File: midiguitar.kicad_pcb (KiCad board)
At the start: 2 copper layers, 64.9 x 24.8 mm, 12 parts, among them M1 ESP32S3, P1 Conn_USB_A_Plug, SW1 Switch_Slide_1, SW2 Switch_Slide_1, U1 Regulator_Linear_3.3V_1A_Diod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, U2 LevelShifter_Texas_TXB0104DR_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

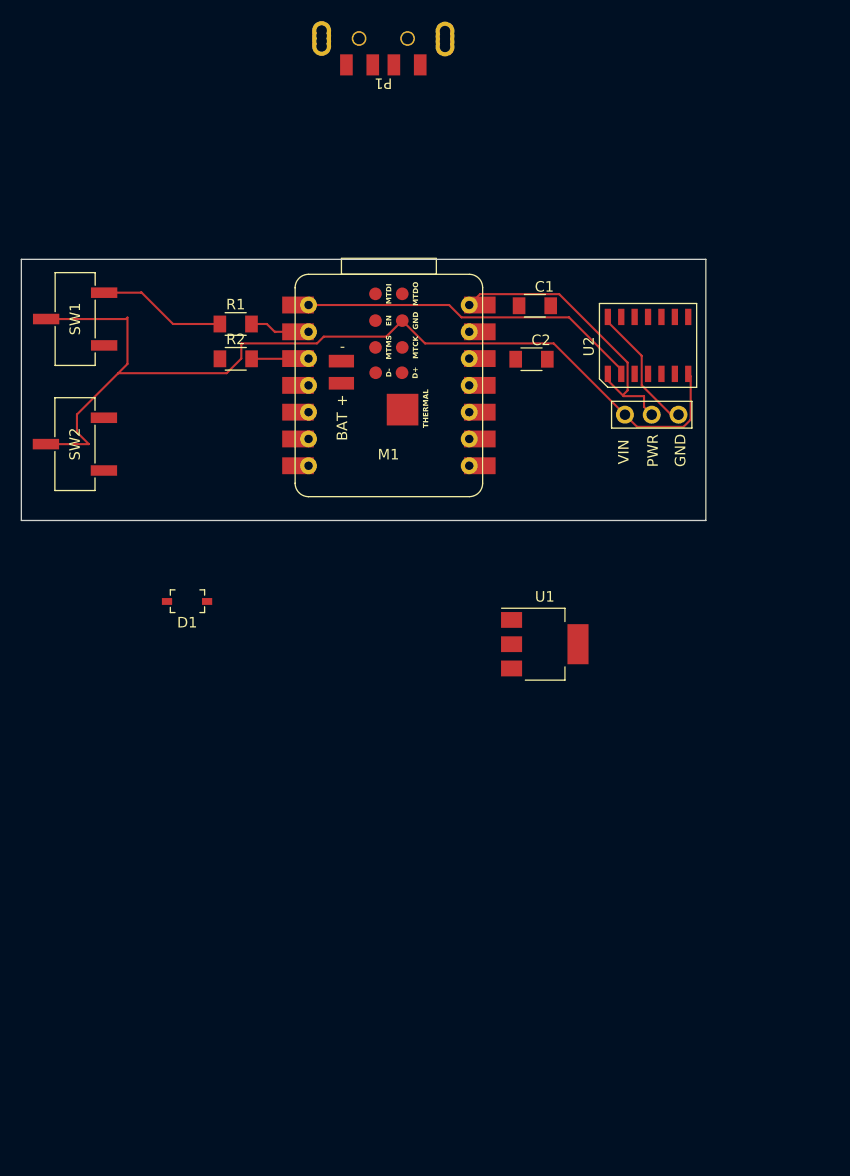
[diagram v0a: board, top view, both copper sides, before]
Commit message: Update sym-lib-table version to 7 for midiguitar-eagle-import library
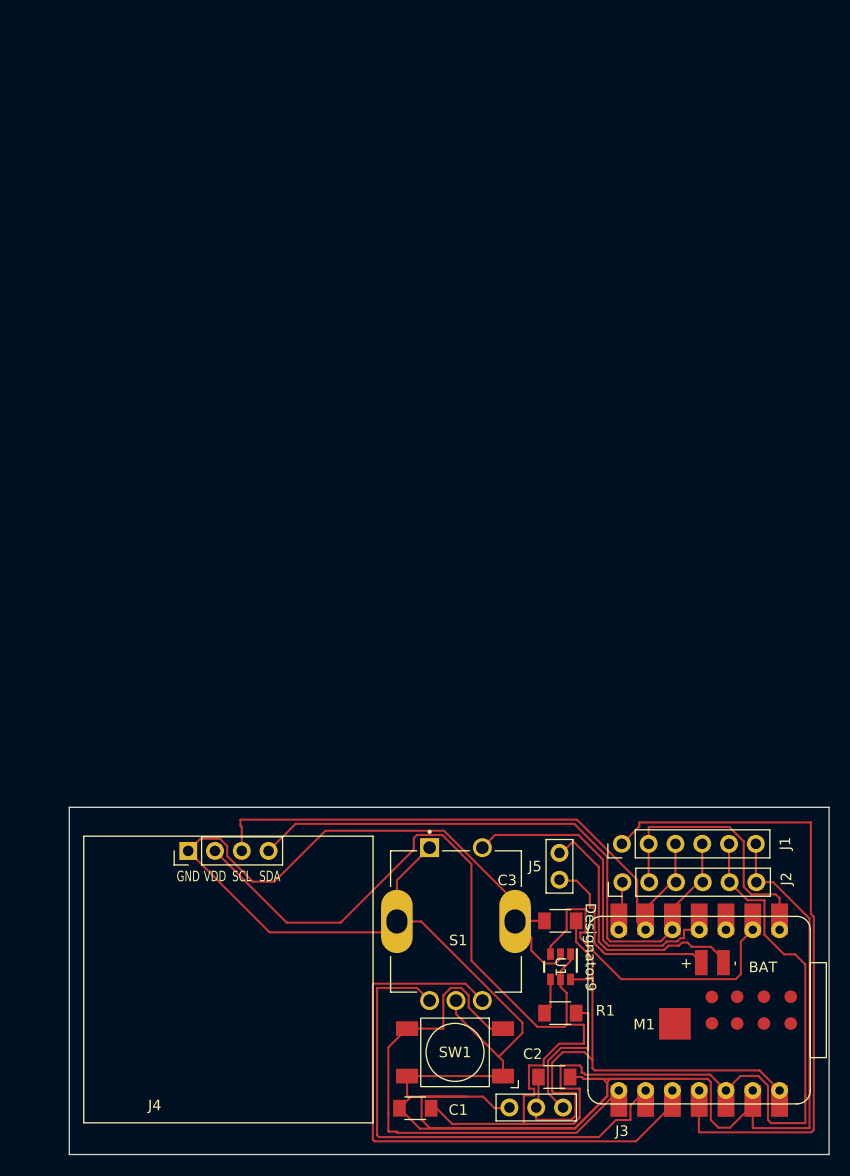
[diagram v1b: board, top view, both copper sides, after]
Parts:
- removed D1: Diode_Schottky_SOD123, PCM_fab:Diode_Schottky_SOD123
- removed GND: PinHeader_NeoPixel_16Led, PCM_fab:PinHeader_01x03_P2.54mm_Vertical_THT_D1mm
- removed P1: Conn_USB_A_Plug, PCM_fab:Conn_USB_A_Plug
- removed R2: 10k, PCM_fab:R_1206
- removed SW2: Switch_Slide_1, PCM_fab:Switch_Slide_Top_CnK_JS102011SCQN_8.5x3.5mm
- removed U2: LevelShifter_Texas_TXB0104DR_SOIC-14, PCM_fab:LevelShifter_Texas_TXB0104DR_SOIC-14
- added C3: 100uF, PCM_fab:C_1206, F.Cu at (161.7, 130.6)
- added J1: PinHeader_01x06_P2.54mm_Vertical_THT_D1mm, PCM_fab:PinHeader_01x06_P2.54mm_Vertical_THT_D1mm, F.Cu at (167.5, 123.3)
- added J2: PinHeader_01x06_P2.54mm_Vertical_THT_D1mm, PCM_fab:PinHeader_01x06_P2.54mm_Vertical_THT_D1mm, F.Cu at (167.6, 126.9)
- added J3: NeoPixel, PCM_fab:PinHeader_01x03_P2.54mm_Vertical_THT_D1mm, F.Cu at (161.9, 148.3)
- added J4: Oled Display, footprints:Display_128x64_096_I2C, F.Cu at (130.2, 124.0)
- added J5: ~, PCM_fab:PinHeader_01x02_P2.54mm_Vertical_THT_D1mm, F.Cu at (161.6, 124.2)
- added S1: PEC12R-4015F-S0024, PEC12R-4015F-S0024:XDCR_PEC12R-4015F-S0024, F.Cu at (151.8, 130.7)
- C1, C2: value C_1206 -> 100nF
- R1: value 10k -> 330
- SW1: value Switch_Slide_1 -> Switch_Tactile_CUIDevices; footprint PCM_fab:Switch_Slide_Top_CnK_JS102011SCQN_8.5x3.5mm -> PCM_fab:Button_CUIDevices_TS04-66-43-BK-260-SMT_6.0x6.0mm
- U1: value Regulator_Linear_3.3V_1A_DiodesIncorporated -> SN74LVC1T45DBVR; footprint PCM_fab:SOT-223-3_TabPin2 -> footprints:DBV0006A_N
- moved SW1 78.3 mm to (151.7, 143.1), turned to 180 degrees
- moved C1 76.9 mm to (147.9, 148.4), turned to 180 degrees
- moved R1 72.2 mm to (161.7, 139.3)
- moved C2 68.1 mm to (161.1, 145.4)
- moved M1 66.1 mm to (174.8, 139.1), turned to -90 degrees
- moved U1 30.6 mm to (161.7, 134.9), turned to -90 degrees
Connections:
- C1 pad 1: unconnected-(C1-Pad1) -> PWR_3V3
- C1 pad 2: unconnected-(C1-Pad2) -> PWR_GND
- C2 pad 1: unconnected-(C2-Pad1) -> PWR_5V
- C2 pad 2: unconnected-(C2-Pad2) -> PWR_GND
- M1 pad 1: Net-(M1-D0) -> INT
- M1 pad 10: unconnected-(M1-D9-Pad10) -> Net-(M1-D9)
- M1 pad 11: unconnected-(M1-D10-Pad11) -> XSHUT
- M1 pad 13: unconnected-(M1-GND-Pad13) -> PWR_GND
- M1 pad 15: unconnected-(M1-BAT_GND-Pad15) -> Net-(J5-Pin_1)
- M1 pad 16: unconnected-(M1-BAT_VIN-Pad16) -> Net-(J5-Pin_2)
- M1 pad 21: Net-(GND1-Pin_3) -> unconnected-(M1-GND-Pad21)
- M1 pad 23: Net-(M1-D-) -> unconnected-(M1-D--Pad23)
- M1 pad 24: Net-(M1-D+) -> unconnected-(M1-D+-Pad24)
- M1 pad 3: Net-(M1-D2) -> unconnected-(M1-D2-Pad3)
- M1 pad 5: Net-(M1-D4) -> SDA
- M1 pad 6: unconnected-(M1-D5-Pad6) -> SCL
- M1 pad 7: SDA -> XSHUT_2
- M1 pad 8: SCL -> Net-(M1-D7)
- M1 pad 9: unconnected-(M1-D8-Pad9) -> Net-(M1-D8)
- R1 pad 1: Net-(SW1-C) -> Net-(U1-B)
- R1 pad 2: Net-(M1-D1) -> Net-(J3-Pin_1)
- SW1 pad 1: unconnected-(SW1-A-Pad1) -> PWR_GND
- SW1 pad 2: Net-(GND1-Pin_3) -> PWR_GND
- SW1 pad 3: Net-(SW1-C) -> Net-(M1-D7)
- U1 pad 1: unconnected-(U1-GND-Pad1) -> PWR_3V3
- U1 pad 2: unconnected-(U1-VO-Pad2) -> PWR_GND
- U1 pad 3: unconnected-(U1-VI-Pad3) -> Net-(M1-D1)
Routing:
- net PWR_GND: track 0.00 -> 257.6 mm
- net PWR_3V3: track 0.00 -> 160.0 mm
- net Net-(GND1-Pin_3): track 92.4 -> 0.00 mm
- net XSHUT: track 0.00 -> 63.2 mm
- net SDA: track 0.00 -> 58.6 mm
- net SCL: track 0.00 -> 57.8 mm
- net Net-(M1-D9): track 0.00 -> 57.1 mm
- net Net-(M1-D7): track 0.00 -> 49.0 mm
- net Net-(M1-D8): track 0.00 -> 47.6 mm
- net Net-(M1-D0): track 32.6 -> 0.00 mm
- net Net-(M1-D3): track 0.00 -> 31.0 mm
- net PWR_5V: track 28.0 -> 55.4 mm
- net INT: track 0.00 -> 26.0 mm
- net Net-(M1-D1): track 5.74 -> 31.6 mm
- net Net-(J5-Pin_1): track 0.00 -> 25.6 mm
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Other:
- board size 64.9 x 24.8 mm -> 72 x 32.9 mm
- board text removed: "PWR"
- board text removed: "VIN"
